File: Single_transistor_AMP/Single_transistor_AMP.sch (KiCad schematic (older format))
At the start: 18 parts, among them J1 Power_Supply, J2 Signal_In, J3 Signal_Out, Q1 BC548, Q2 BC548

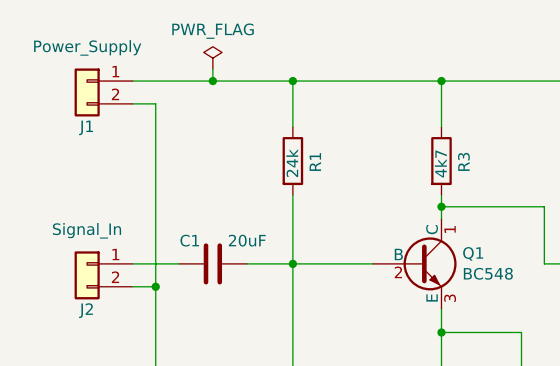
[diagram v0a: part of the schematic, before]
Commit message: Single_Transistor_AMP PCB Layout created
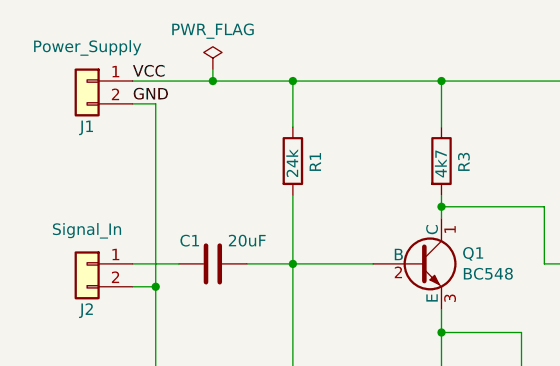
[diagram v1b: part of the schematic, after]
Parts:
- R1, R2, R3, R4, R5, R6, R7, R8: footprint Resistors_SMD:R_0805_HandSoldering -> Resistors_SMD:R_1206_HandSoldering
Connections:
- net GND: now reaches C2.1, C5.1, J1.2 (Pin_2), J2.2 (Pin_2), J3.2 (Pin_2), R2.2, R4.2, R6.2, R8.2
- net VCC: now reaches J1.1 (Pin_1), R1.1, R3.1, R5.1, R7.1
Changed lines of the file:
@@
 EESchema Schematic File Version 4
+LIBS:Single_transistor_AMP-cache
 EELAYER 26 0
 EELAYER END
@@
 F 0 "R2" V 2650 3800 50  0000 L CNN
 F 1 "6k8" V 2550 3775 50  0000 L CNN
-F 2 "Resistors_SMD:R_0805_HandSoldering" V 2480 3850 50  0001 C CNN
+F 2 "Resistors_SMD:R_1206_HandSoldering" V 2480 3850 50  0001 C CNN
 F 3 "https://eu.mouser.com/datasheet/2/315/Panasonic_Resistors_Thick_Film_Anti_Sulf_Anti_Surg-1825099.pdf" H 2550 3850 50  0001 C CNN
 	1    2550 3850
@@
 F 0 "R1" V 2650 2750 50  0000 L CNN
 F 1 "24k" V 2550 2725 50  0000 L CNN
-F 2 "Resistors_SMD:R_0805_HandSoldering" V 2480 2800 50  0001 C CNN
+F 2 "Resistors_SMD:R_1206_HandSoldering" V 2480 2800 50  0001 C CNN
 F 3 "https://eu.mouser.com/datasheet/2/315/Panasonic_Resistors_Thick_Film_Anti_Sulf_Anti_Surg-1825099.pdf" H 2550 2800 50  0001 C CNN
 	1    2550 2800
@@
 F 0 "R3" V 3300 2750 50  0000 L CNN
 F 1 "4k7" V 3200 2725 50  0000 L CNN
-F 2 "Resistors_SMD:R_0805_HandSoldering" V 3130 2800 50  0001 C CNN
+F 2 "Resistors_SMD:R_1206_HandSoldering" V 3130 2800 50  0001 C CNN
 F 3 "https://eu.mouser.com/datasheet/2/315/Panasonic_Resistors_Thick_Film_Anti_Sulf_Anti_Surg-1825099.pdf" H 3200 2800 50  0001 C CNN
 	1    3200 2800
@@
 F 0 "R4" V 3300 3800 50  0000 L CNN
 F 1 "1k8" V 3200 3775 50  0000 L CNN
-F 2 "Resistors_SMD:R_0805_HandSoldering" V 3130 3850 50  0001 C CNN
+F 2 "Resistors_SMD:R_1206_HandSoldering" V 3130 3850 50  0001 C CNN
 F 3 "https://eu.mouser.com/datasheet/2/315/Panasonic_Resistors_Thick_Film_Anti_Sulf_Anti_Surg-1825099.pdf" H 3200 3850 50  0001 C CNN
 	1    3200 3850
@@
 F 0 "R6" V 4550 3800 50  0000 L CNN
 F 1 "6k8" V 4450 3775 50  0000 L CNN
-F 2 "Resistors_SMD:R_0805_HandSoldering" V 4380 3850 50  0001 C CNN
+F 2 "Resistors_SMD:R_1206_HandSoldering" V 4380 3850 50  0001 C CNN
 F 3 "https://eu.mouser.com/datasheet/2/315/Panasonic_Resistors_Thick_Film_Anti_Sulf_Anti_Surg-1825099.pdf" H 4450 3850 50  0001 C CNN
 	1    4450 3850
@@
 F 0 "R5" V 4550 2750 50  0000 L CNN
 F 1 "24k" V 4450 2725 50  0000 L CNN
-F 2 "Resistors_SMD:R_0805_HandSoldering" V 4380 2800 50  0001 C CNN
+F 2 "Resistors_SMD:R_1206_HandSoldering" V 4380 2800 50  0001 C CNN
 F 3 "https://eu.mouser.com/datasheet/2/315/Panasonic_Resistors_Thick_Film_Anti_Sulf_Anti_Surg-1825099.pdf" H 4450 2800 50  0001 C CNN
 	1    4450 2800
@@
 F 0 "R7" V 5200 2750 50  0000 L CNN
 F 1 "4k7" V 5100 2725 50  0000 L CNN
-F 2 "Resistors_SMD:R_0805_HandSoldering" V 5030 2800 50  0001 C CNN
+F 2 "Resistors_SMD:R_1206_HandSoldering" V 5030 2800 50  0001 C CNN
 F 3 "https://eu.mouser.com/datasheet/2/315/Panasonic_Resistors_Thick_Film_Anti_Sulf_Anti_Surg-1825099.pdf" H 5100 2800 50  0001 C CNN
 	1    5100 2800
@@
 F 0 "R8" V 5200 3800 50  0000 L CNN
 F 1 "1k8" V 5100 3775 50  0000 L CNN
-F 2 "Resistors_SMD:R_0805_HandSoldering" V 5030 3850 50  0001 C CNN
+F 2 "Resistors_SMD:R_1206_HandSoldering" V 5030 3850 50  0001 C CNN
 F 3 "https://eu.mouser.com/datasheet/2/315/Panasonic_Resistors_Thick_Film_Anti_Sulf_Anti_Surg-1825099.pdf" H 5100 3850 50  0001 C CNN
 	1    5100 3850
@@
 	6000 4100 5450 4100
 Connection ~ 5450 4100
+Text Label 1850 2550 0    50   ~ 0
+GND
+Text Label 1850 2450 0    50   ~ 0
+VCC
 $EndSCHEMATC
